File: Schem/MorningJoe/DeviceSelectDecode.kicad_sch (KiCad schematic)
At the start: 11 parts, among them SW1 SW_Coded_SH-7070, U11 74HC688

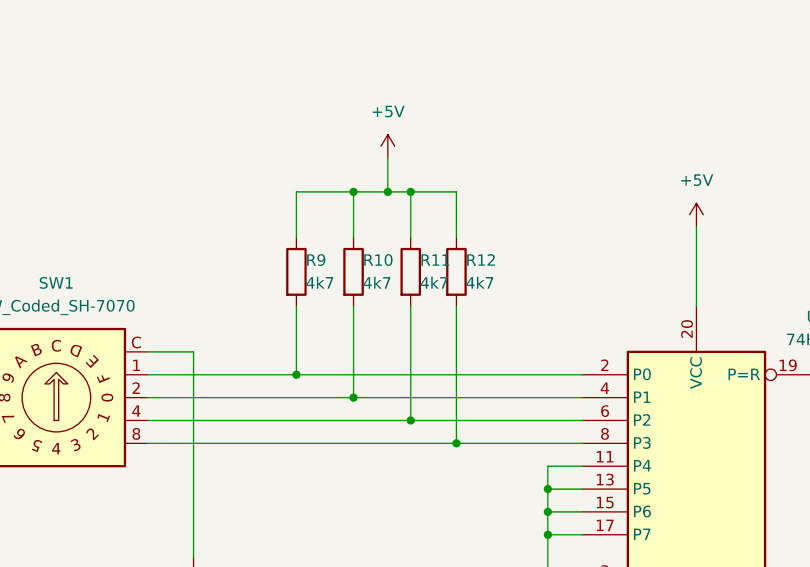
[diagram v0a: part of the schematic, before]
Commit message: Added both the Morning Joe and the Lunch Crema schematics, PCB, and KiCad library files.
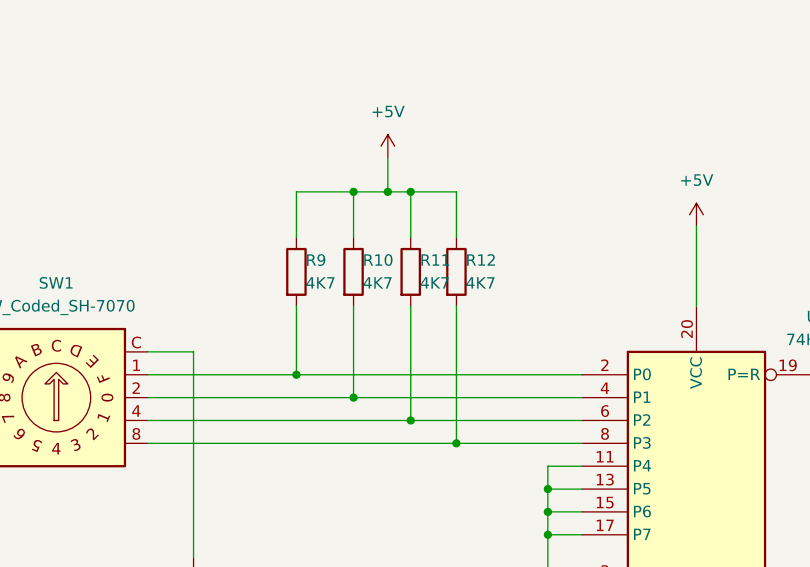
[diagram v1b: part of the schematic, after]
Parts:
- R10, R11, R12, R9: value 4k7 -> 4K7
- SW1: MANUFACTURER_PART_NUMBER SH-7070TB -> SH-7070MC
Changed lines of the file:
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@@
 			)
 		)
-		(property "Value" "4k7"
+		(property "Value" "4K7"
 			(at 98.806 78.74 0)
 			(show_name no)
@@
 			)
 		)
-		(property "Value" "4k7"
+		(property "Value" "4K7"
 			(at 92.456 78.74 0)
 			(show_name no)
@@
 			)
 		)
-		(property "Value" "4k7"
+		(property "Value" "4K7"
 			(at 86.106 78.74 0)
 			(show_name no)
@@
 			)
 		)
-		(property "MANUFACTURER_PART_NUMBER" "SH-7070TB"
+		(property "MANUFACTURER_PART_NUMBER" "SH-7070MC"
 			(at 58.42 91.44 0)
 			(hide yes)
@@
 			)
 		)
-		(property "Value" "4k7"
+		(property "Value" "4K7"
 			(at 103.886 78.74 0)
 			(show_name no)
